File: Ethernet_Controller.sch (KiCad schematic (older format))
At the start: 31 parts, among them J1 5-2337992-8, U1 RTL8111H, Y1 ABM8G-25.000MHZ-18-D2Y-T

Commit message: Cleanign Ethernet_Controller.sch
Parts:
- added C?: C_100n_0402, sa800u-baseboard-hw-footprints:0402-cap, symbol sa800u-baseboard-hw:C_100n_0402
- added C?: C_4u7_0402, sa800u-baseboard-hw-footprints:0402-cap, symbol sa800u-baseboard-hw:C_4u7_0402
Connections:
- net labels added: 1V8_SYS, 3V3_SYS
- net labels removed: 1V8, 3V3
- wire segments 149 -> 169
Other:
- note added: "Possible replacement:\nhttps://www.l-p.com/products/457392.htm"
- note removed: "4u7 caps should be \nplaced near pins ..."
- note removed: "Ethernet connector have built in magnetics. \nIs using separate transformer intentional?\nUse connector without magnetics or change to connector \nwith magnetics and POE"
- note removed: "RJ45 chineese replacement. \nhttps://www.l-p.com/products/457392.htm"
- note removed: "There are 3 power input pins connected to 3V3.\nOne 100nF cap is missing"
- note removed: "Try to add 15K resistor in 0402 package,\nadd it to library using provided script.\nThis will simplify layout."
- moved on the sheet: C1, C10, C12, C15, C17, C18, C19, C2, C20, C21, C3, C4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

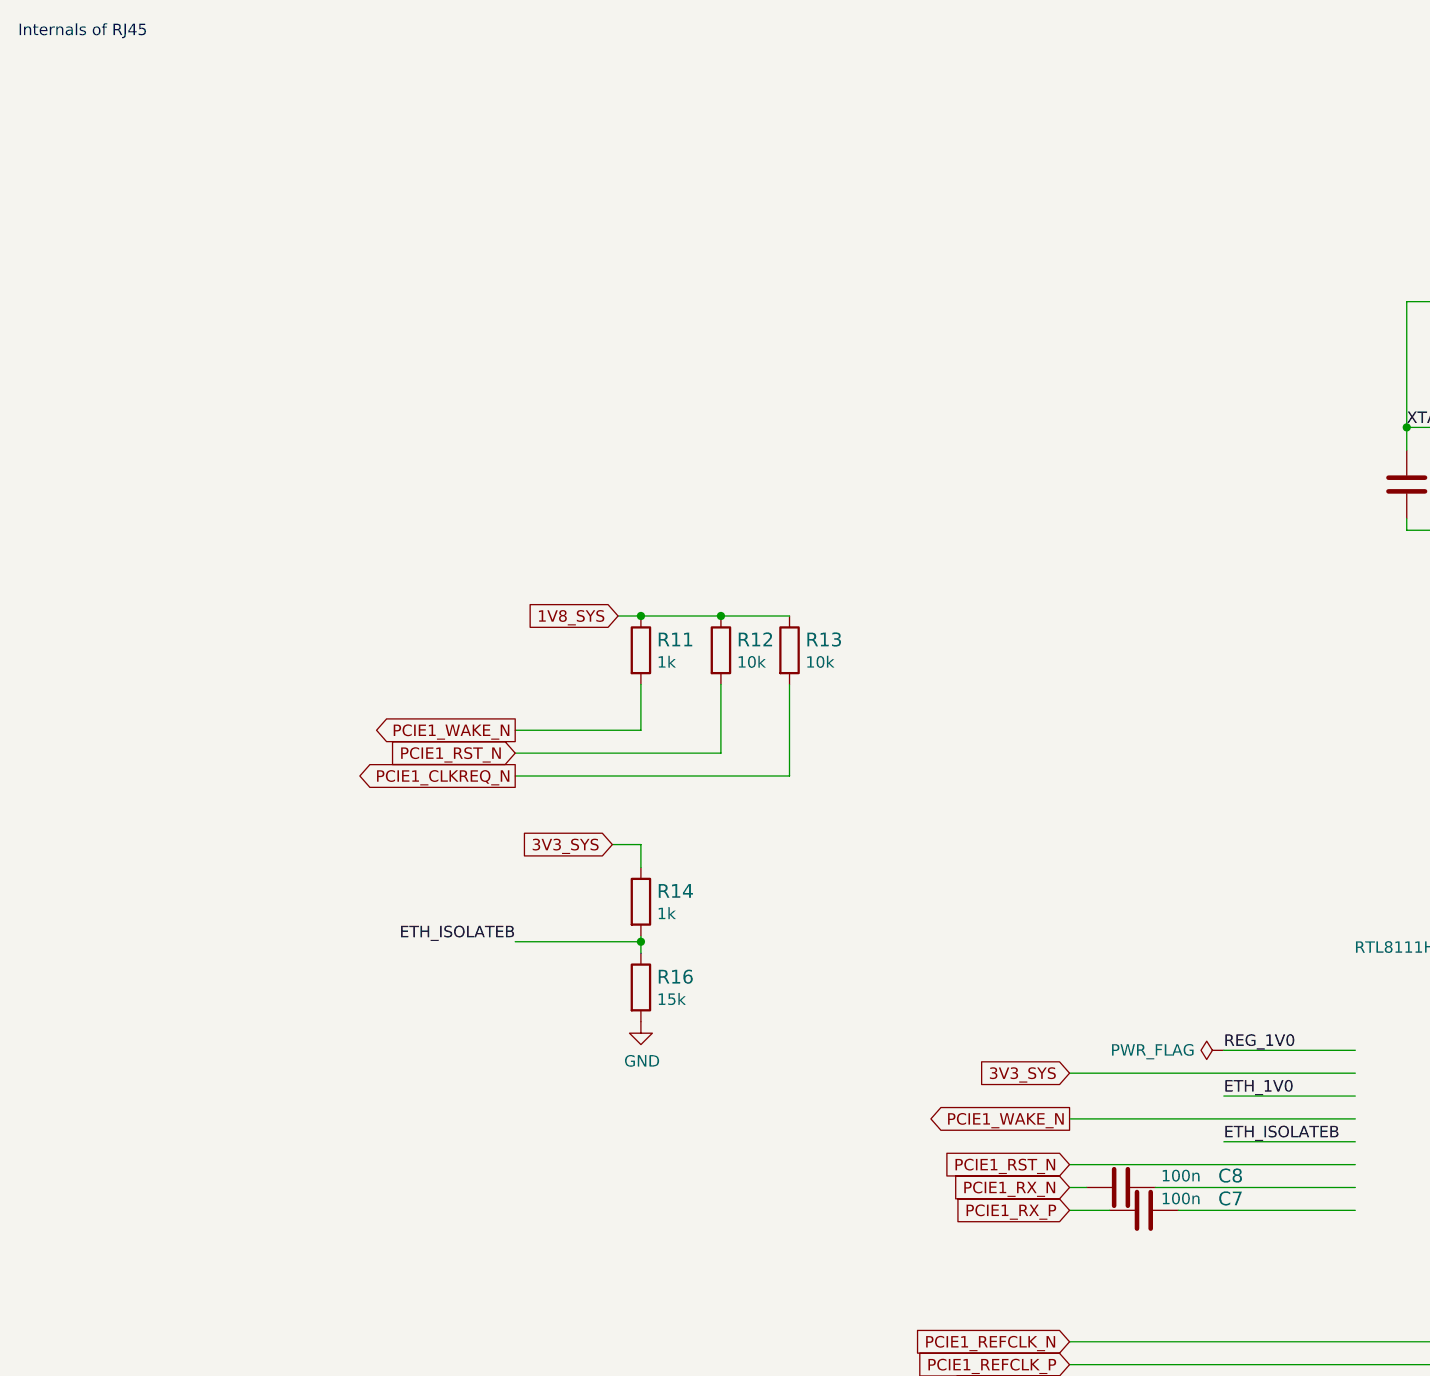
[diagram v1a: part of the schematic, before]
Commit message: Fix C8 and C7 ref positions
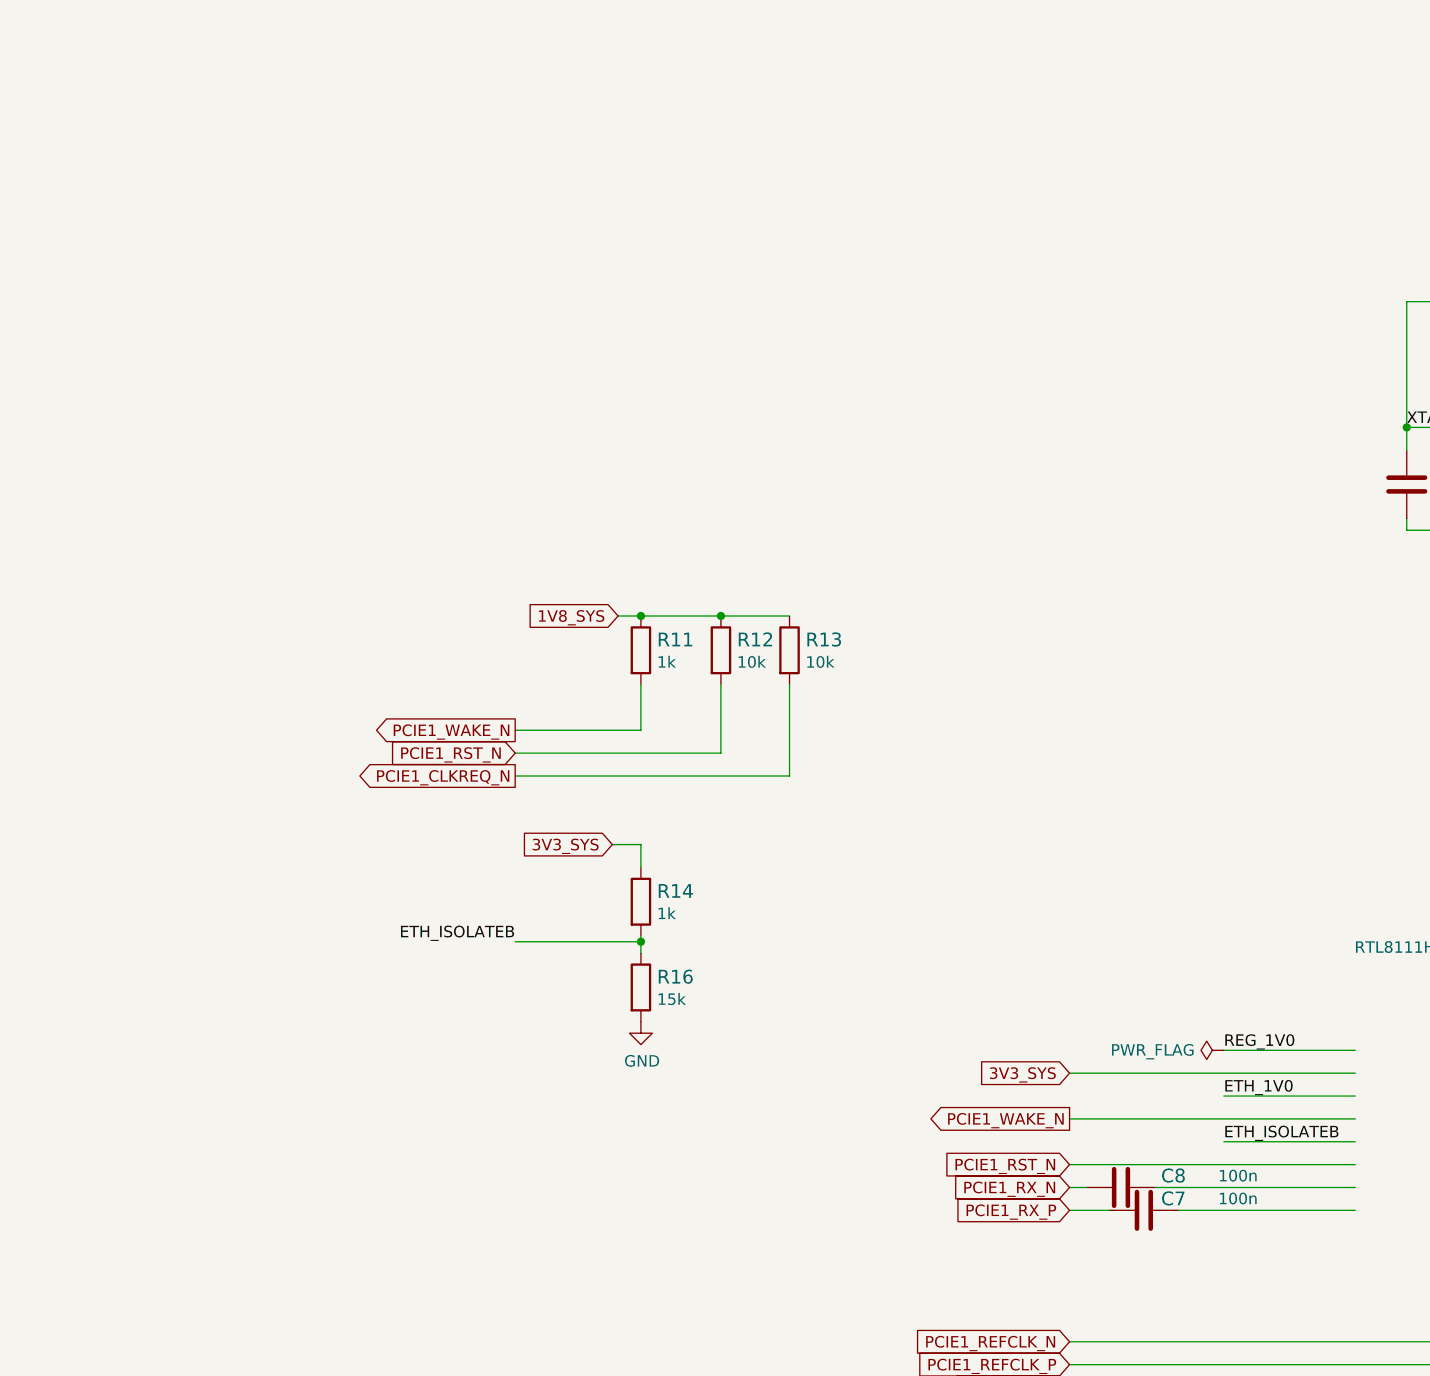
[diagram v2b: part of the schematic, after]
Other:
- note removed: "Internals of RJ45"
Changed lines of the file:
@@
 Comment4 ""
 $EndDescr
-Text Notes 1500 750  0    50   ~ 0
-Internals of RJ45
 $Comp
 L sa800u-baseboard-hw:ABM8G-25.000MHZ-18-D2Y-T Y1
@@
 U 1 1 6190876E
 P 6325 5775
-F 0 "C8" V 6275 5350 60  0000 R CNN
+F 0 "C8" V 6275 5600 60  0000 R CNN
 F 1 "C_100n_0402" H 6325 5625 60  0001 C CNN
 F 2 "sa800u-baseboard-hw-footprints:0402-cap" H 6525 5975 60  0001 L CNN
@@
 F 4 "Walsin" H 6525 6175 60  0001 L CNN "Manufacturer"
 F 5 "0402X104K6R3CT" H 6525 6075 60  0001 L CNN "MPN"
-F 6 "100n" V 6275 5600 50  0000 R CNN "Val"
+F 6 "100n" V 6275 5350 50  0000 R CNN "Val"
 	1    6325 5775
 	0    -1   1    0
@@
 U 1 1 61907765
 P 6425 5875
-F 0 "C7" V 6375 5550 60  0000 R CNN
+F 0 "C7" V 6375 5800 60  0000 R CNN
 F 1 "C_100n_0402" H 6425 5725 60  0001 C CNN
 F 2 "sa800u-baseboard-hw-footprints:0402-cap" H 6625 6075 60  0001 L CNN
@@
 F 4 "Walsin" H 6625 6275 60  0001 L CNN "Manufacturer"
 F 5 "0402X104K6R3CT" H 6625 6175 60  0001 L CNN "MPN"
-F 6 "100n" V 6375 5800 50  0000 R CNN "Val"
+F 6 "100n" V 6375 5550 50  0000 R CNN "Val"
 	1    6425 5875
 	0    -1   1    0

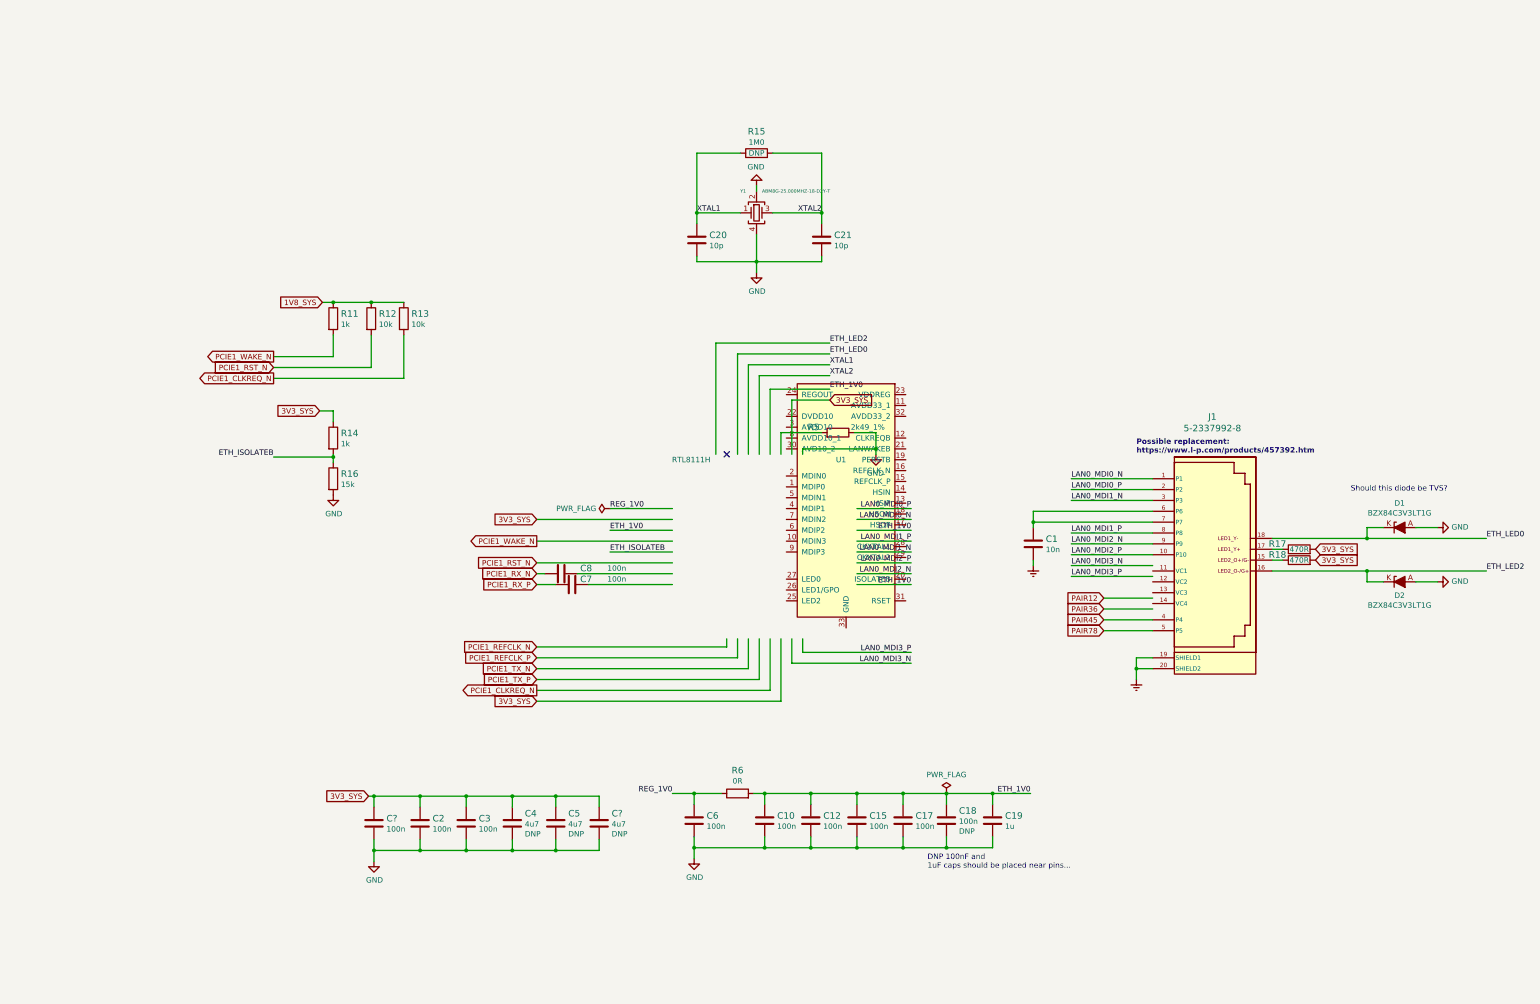
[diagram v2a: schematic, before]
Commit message: Update Ethernet_Controller.sch, tweak RTL8111H for simpler schematic
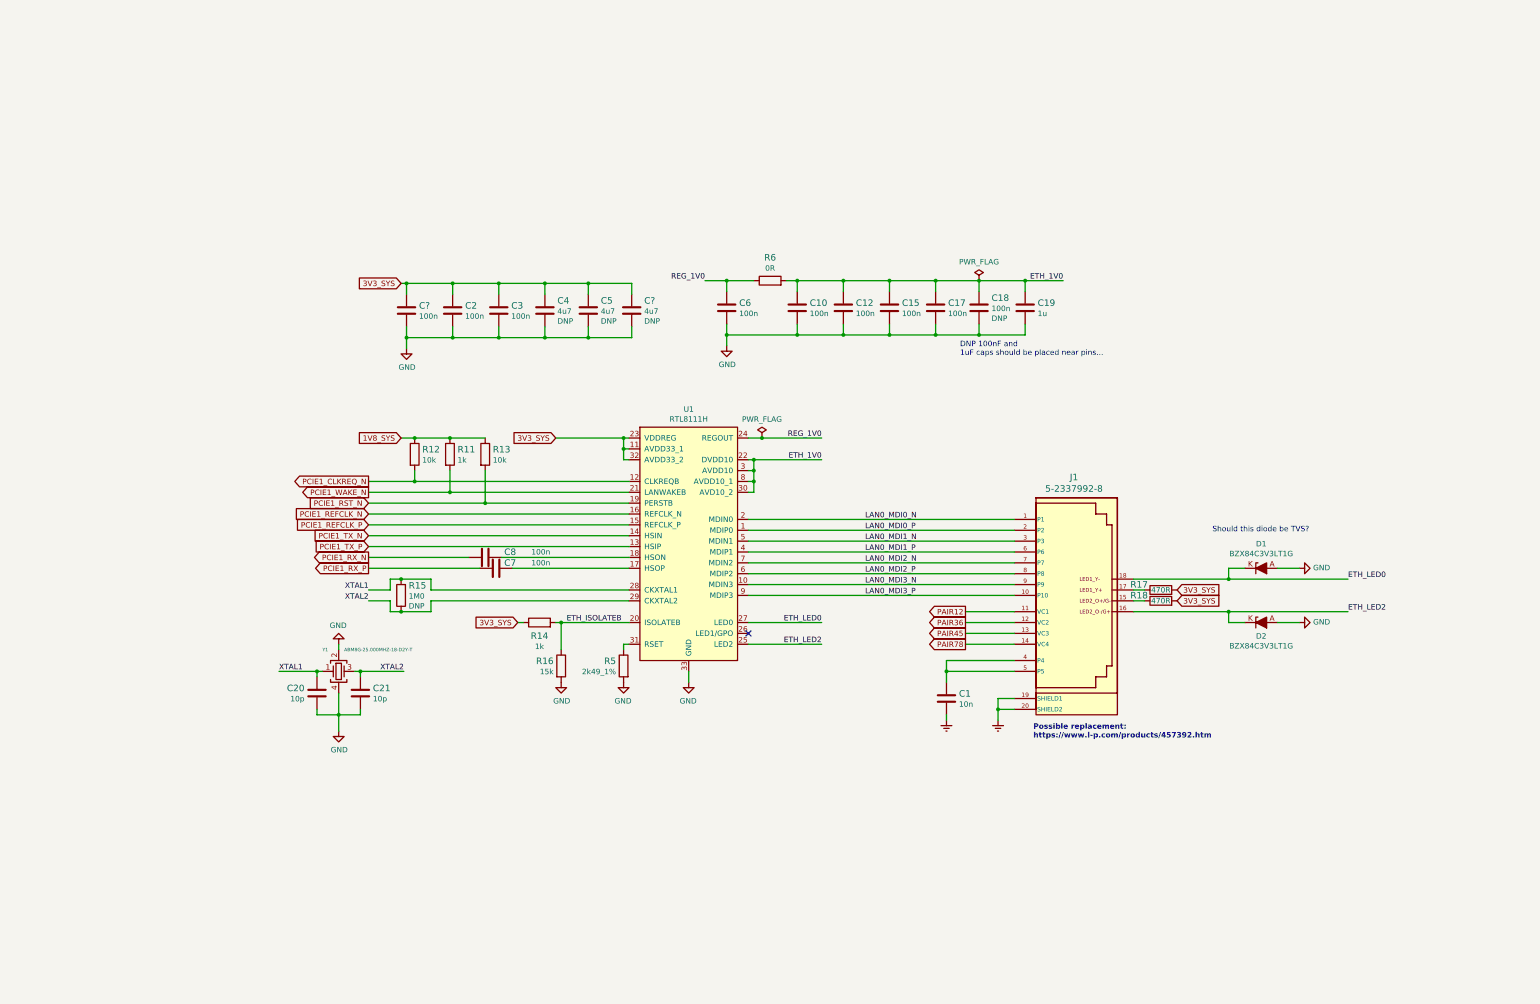
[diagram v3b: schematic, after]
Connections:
- wire segments 169 -> 157
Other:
- moved on the sheet: C1, C10, C12, C15, C17, C18, C19, C2, C20, C21, C3, C4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

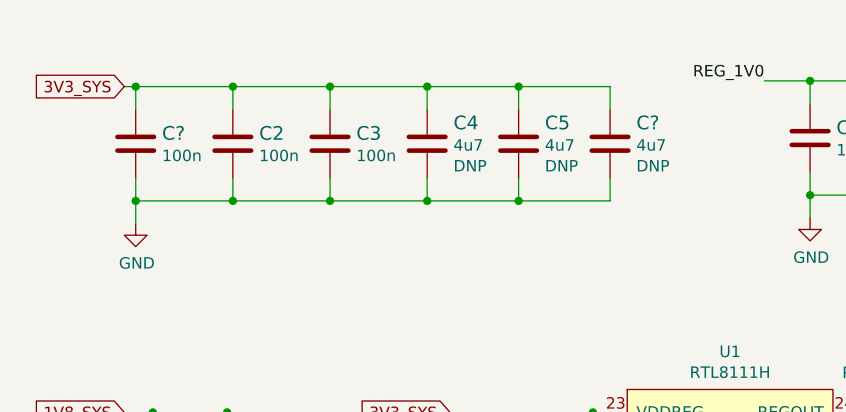
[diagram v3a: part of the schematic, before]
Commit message: Annotate parts
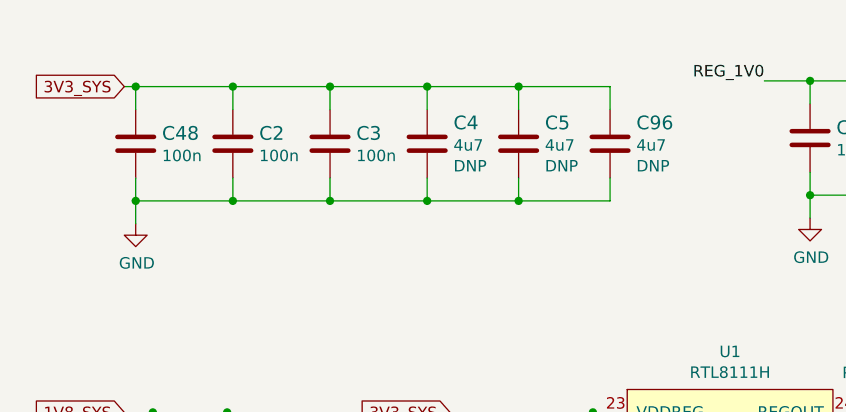
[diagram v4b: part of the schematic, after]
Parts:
- gave numbers to parts that had none: 2
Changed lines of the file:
@@
 DNP 100nF and \n1uF caps should be placed near pins...
 $Comp
-L sa800u-baseboard-hw:C_100n_0402 C?
+L sa800u-baseboard-hw:C_100n_0402 C48
 U 1 1 61E50090
 P 4900 3350
-F 0 "C?" H 5015 3395 60  0000 L CNN
+F 0 "C48" H 5015 3395 60  0000 L CNN
 F 1 "C_100n_0402" H 4900 3200 60  0001 C CNN
 F 2 "sa800u-baseboard-hw-footprints:0402-cap" H 5100 3550 60  0001 L CNN
@@
 	6175 3100 6575 3100
 $Comp
-L sa800u-baseboard-hw:C_4u7_0402 C?
+L sa800u-baseboard-hw:C_4u7_0402 C96
 U 1 1 61EB43EC
 P 6975 3350
-F 0 "C?" H 7090 3441 60  0000 L CNN
+F 0 "C96" H 7090 3441 60  0000 L CNN
 F 1 "C_4u7_0402" H 6975 3200 60  0001 C CNN
 F 2 "sa800u-baseboard-hw-footprints:0402-cap" H 7175 3550 60  0001 L CNN
@@
 $EndComp
 $Comp
-L sa800u-baseboard-hw:PWR_FLAG #FLG?
+L sa800u-baseboard-hw:PWR_FLAG #FLG0101
 U 1 1 62332768
 P 10175 3075
-F 0 "#FLG?" H 10175 3150 50  0001 C CNN
+F 0 "#FLG0101" H 10175 3150 50  0001 C CNN
 F 1 "PWR_FLAG" H 10175 3248 50  0000 C CNN
 F 2 "" H 10175 3075 50  0001 C CNN
@@
 $EndComp
 $Comp
-L sa800u-baseboard-hw:PWR_FLAG #FLG?
+L sa800u-baseboard-hw:PWR_FLAG #FLG0102
 U 1 1 62326493
 P 8175 4525
-F 0 "#FLG?" H 8175 4600 50  0001 C CNN
+F 0 "#FLG0102" H 8175 4600 50  0001 C CNN
 F 1 "PWR_FLAG" H 8175 4698 50  0000 C CNN
 F 2 "" H 8175 4525 50  0001 C CNN
@@
 	6900 6475 6900 6425
 $Comp
-L sa800u-baseboard-hw:GND #PWR?
+L sa800u-baseboard-hw:GND #PWR0145
 U 1 1 631E1DC8
 P 6900 6775
-F 0 "#PWR?" H 6900 6525 50  0001 C CNN
+F 0 "#PWR0145" H 6900 6525 50  0001 C CNN
 F 1 "GND" H 6905 6602 50  0000 C CNN
 F 2 "" H 6900 6775 50  0001 C CNN
